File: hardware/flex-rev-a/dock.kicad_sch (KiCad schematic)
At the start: 11 parts, among them J601 Dock pads

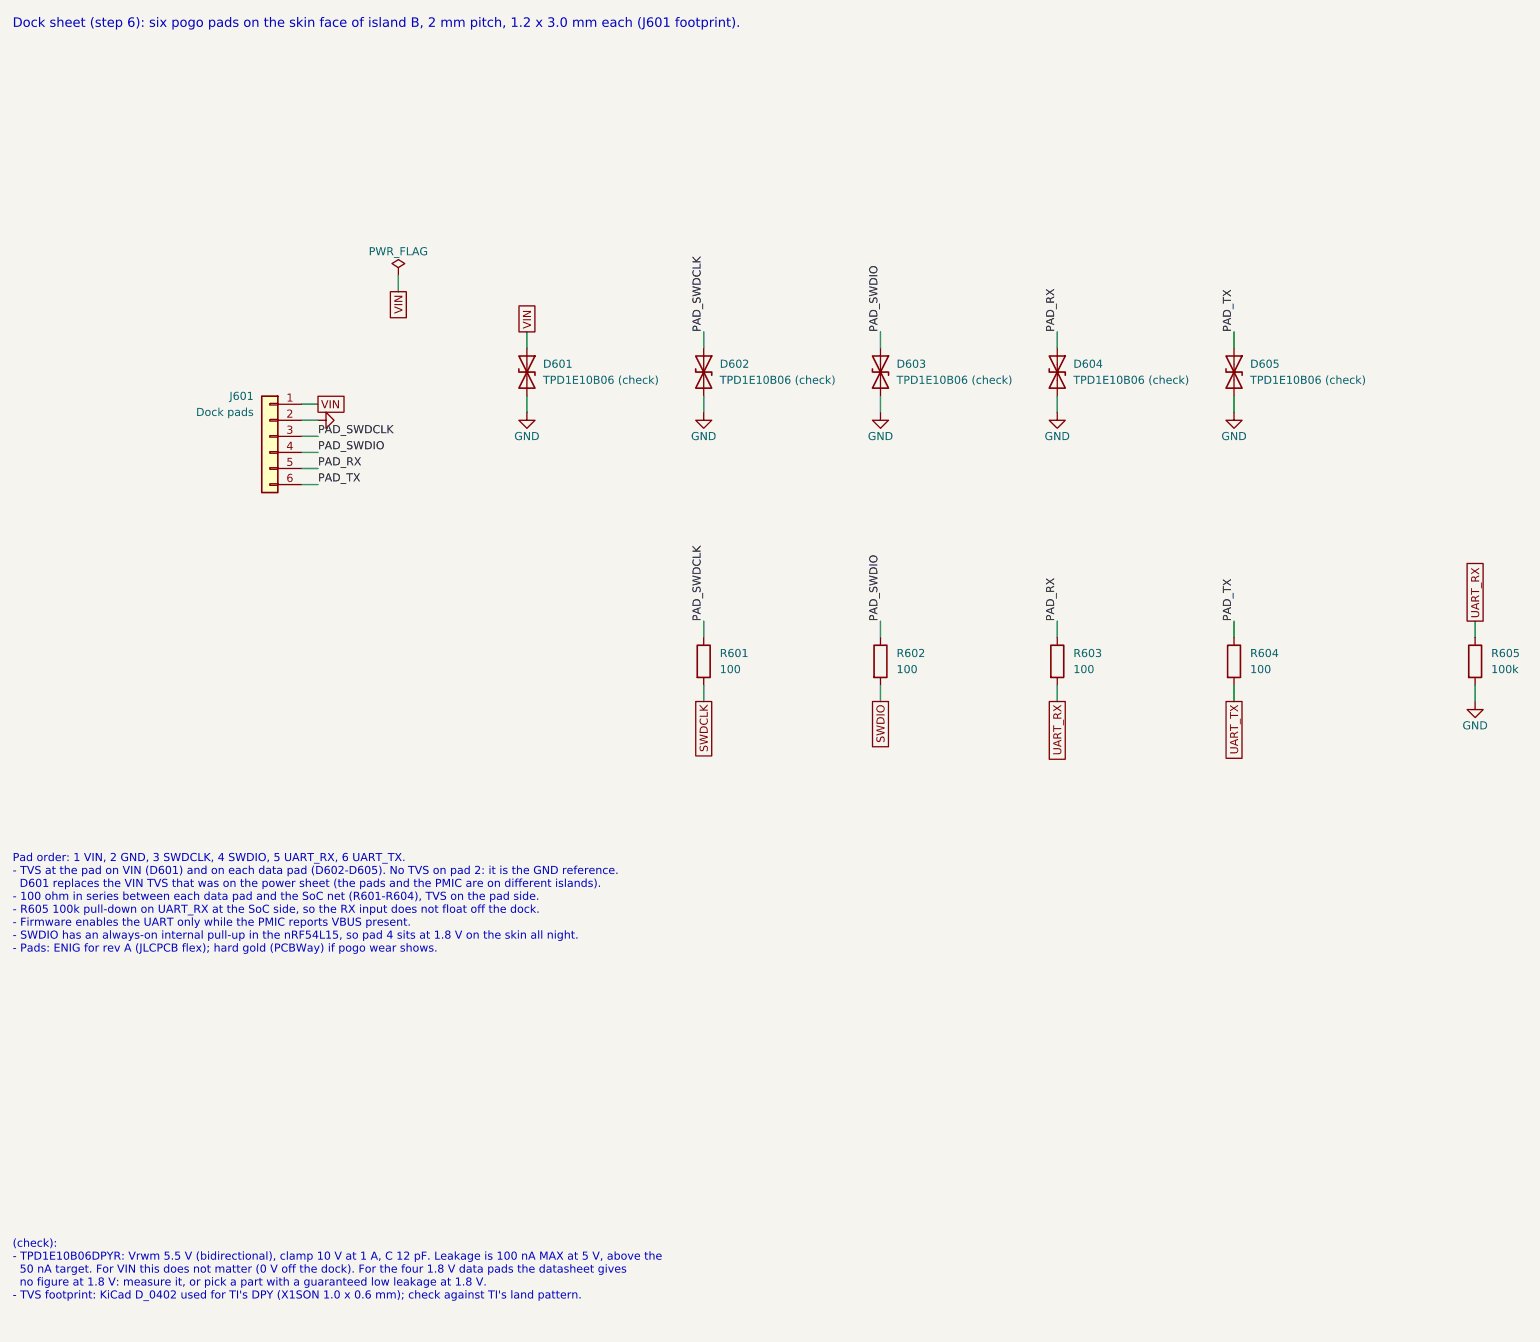
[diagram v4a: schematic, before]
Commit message: Apply schematic review fixes: 2.0 V rail, pad 10 NC, VIN TVS, bulk cap
- Power: R202 47k -> 68k so BUCK1 starts at 2.0 V; global net VDD_1V8
  renamed VDD_2V0 on every sheet, notes updated.
- Haptics: DRV2605L IN/TRIG tied to GND, HAPT_TRIG removed (effects run
  over I2C). Footprint kept as Package_SO:TSSOP-10_3x3mm_P0.5mm: it is
  KiCad's TI DGS land pattern (cites MPDS035); KiCad 10 has no footprint
  named VSSOP-10_3x3mm_P0.5mm.
- MCU: pad 10 (P1.10) no-connect; GND global label replaced by the GND
  power symbol; note on the trapped lower-row GND pads 12/14/16/18 and on
  pads 8/24.
- Sensors: C403 10 uF on LIS2DW12 VDD per ST; related (check) removed.
- Dock: VIN TVS is now Littelfuse SMF18A (SOD-123FL, 18 V standoff, LCSC
  C409420); data pads keep TPD1E10B06, TPD1E0B04 noted as a lower-leakage
  alternative (check).
- bom.csv regenerated, PDF replotted, README updated.

ERC: 0 errors, 0 warnings.

Co-Authored-By: Claude Opus 5.5 <noreply@anthropic.com>
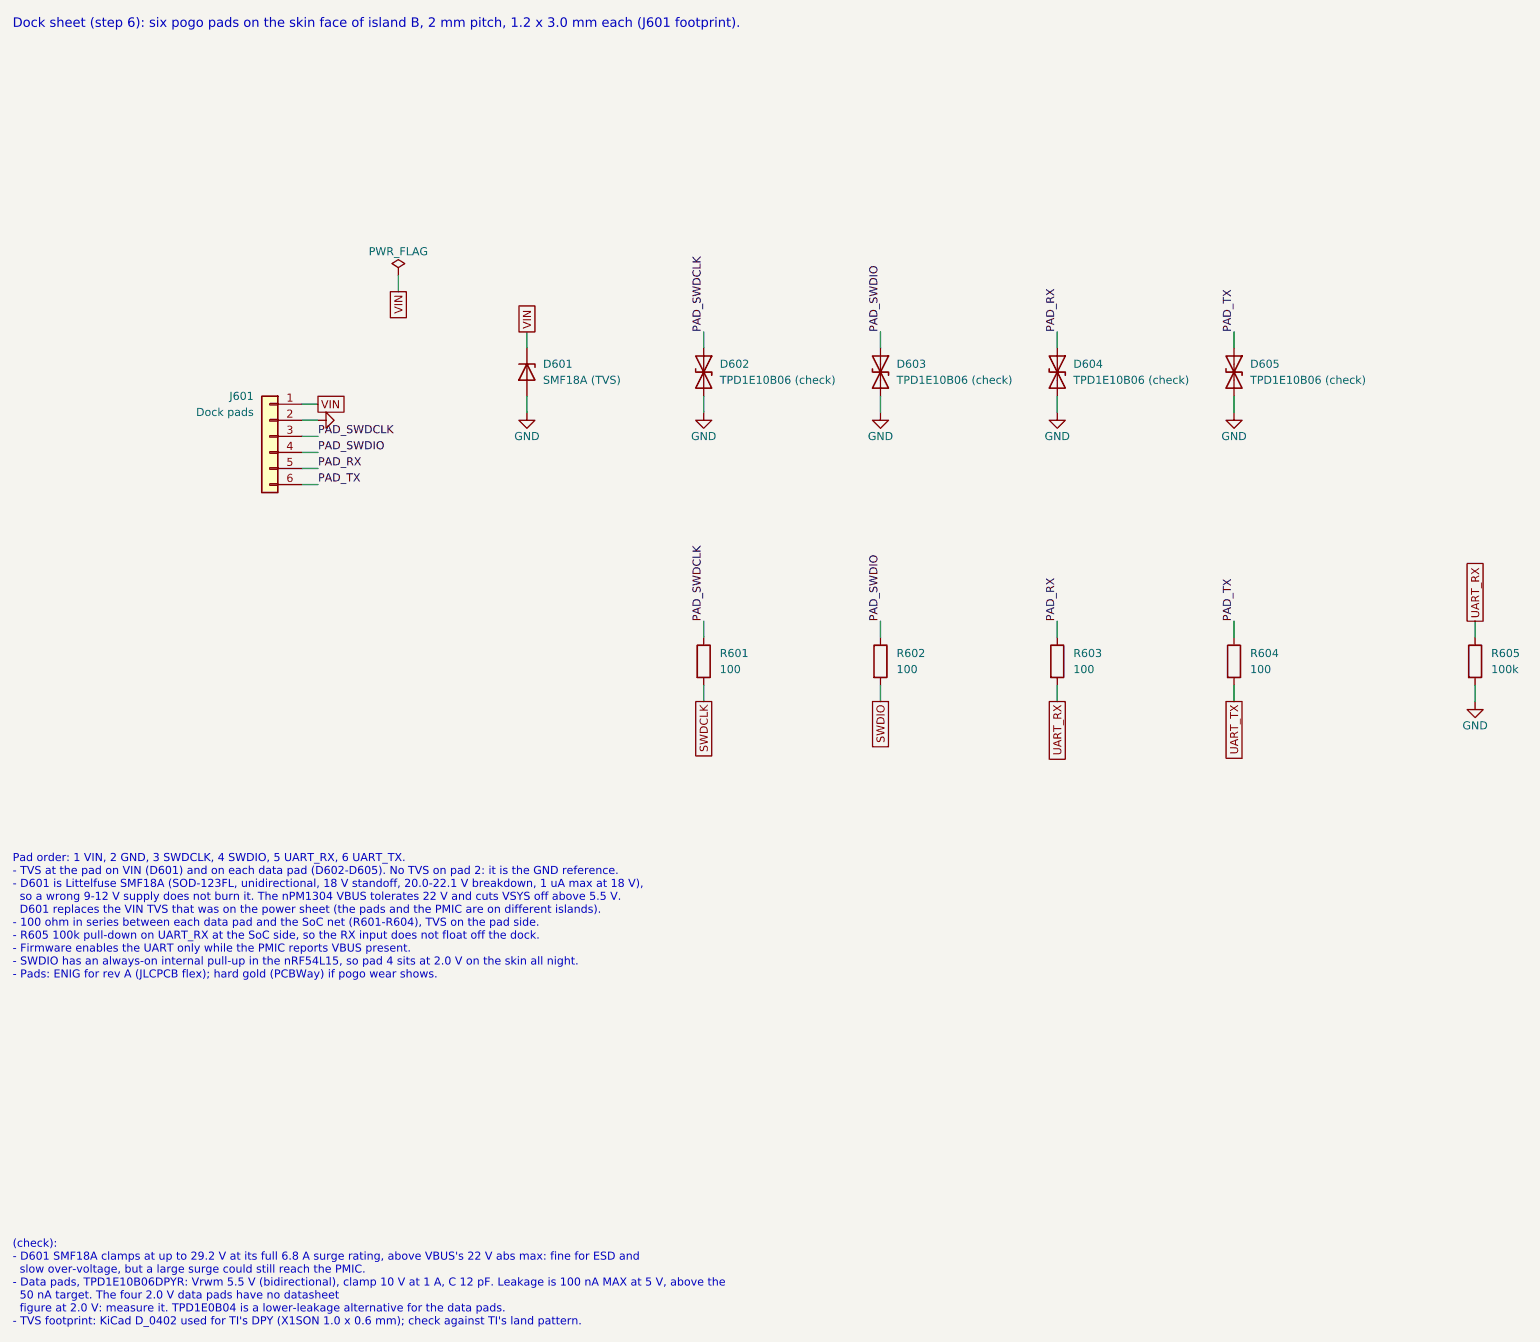
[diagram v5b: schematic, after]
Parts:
- removed D601: TPD1E10B06 (check), Diode_SMD:D_0402_1005Metric, symbol Device:D_TVS
- added D601: SMF18A (TVS), Diode_SMD:D_SOD-123F, symbol Device:D_Zener
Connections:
- net GND: now also D601.2 (A)
- net VIN: now also D601.1 (K)
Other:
- note added: "(check): - D601 SMF18A clamps at up to 29.2 V at its full 6.8 A surge rating, above VBUS's 22 V abs max: fine for ESD and slow over-voltage, but a large surge could still reach the PMIC. - Data pads, TPD1E10B06DPYR: Vrwm 5.5 V (bidirectional), clamp 10 V at 1 A, C 12 pF. Leakage is 100 nA MAX at 5 V, above the 50 nA target. The four 2.0 V data pads have no datasheet figure at 2.0 V: measure it. T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"
- note added: "Pad order: 1 VIN, 2 GND, 3 SWDCLK, 4 SWDIO, 5 UART_RX, 6 UART_TX. - TVS at the pad on VIN (D601) and on each data pad (D602-D605). No TVS on pad 2: it is the GND reference. - D601 is Littelfuse SMF18A (SOD-123FL, unidirectional, 18 V standoff, 20.0-22.1 V breakdown, 1 uA max at 18 V), so a wrong 9-12 V supply does not burn it. The nPM1304 VBUS tolerates 22 V and cuts VSYS off above 5.5 V. D601 re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"
- note removed: "(check): - TPD1E10B06DPYR: Vrwm 5.5 V (bidirectional), clamp 10 V at 1 A, C 12 pF. Leakage is 100 nA MAX at 5 V, above the 50 nA target. For VIN this does not matter (0 V off the dock). For the four 1.8 V data pads the datasheet gives no figure at 1.8 V: measure it, or pick a part with a guaranteed low leakage at 1.8 V. - TVS footprint: KiCad D_0402 used for TI's DPY (X1SON 1.0 x 0.6 mm); check a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"
- note removed: "Pad order: 1 VIN, 2 GND, 3 SWDCLK, 4 SWDIO, 5 UART_RX, 6 UART_TX. - TVS at the pad on VIN (D601) and on each data pad (D602-D605). No TVS on pad 2: it is the GND reference. D601 replaces the VIN TVS that was on the power sheet (the pads and the PMIC are on different islands). - 100 ohm in series between each data pad and the SoC net (R601-R604), TVS on the pad side. - R605 100k pull-down on UART_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"
